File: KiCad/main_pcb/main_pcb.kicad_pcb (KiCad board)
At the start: 2 copper layers, 130 x 100 mm, 61 parts, among them J1 Conn_01x07, J2 Conn_01x07, J3 Conn_01x13, J4 Conn_01x06, J5 Conn_01x02, J6 USB_C_Receptacle_USB2.0_14P, SW1 SW_Push, U1 TXB0104D, U2 TXB0104D, U3 TXB0104D, U4 ATmega2560-16A, U5 AMS1117-3.3, U7 CH340C, Y1 Crystal_GND24

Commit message: feat(PCB): Adds two pins header for LED Backlight
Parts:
- added J7: Conn_01x02, Connector_JST:JST_XH_B2B-XH-A_1x02_P2.50mm_Vertical, F.Cu at (120.2, 52.5)
- moved REF** 5.20 mm to (139.6, 115.3)
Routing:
- net /Screens/MAIN_SCREEN_BL-3V3: track 13.7 -> 27.3 mm, vias 2 -> 3

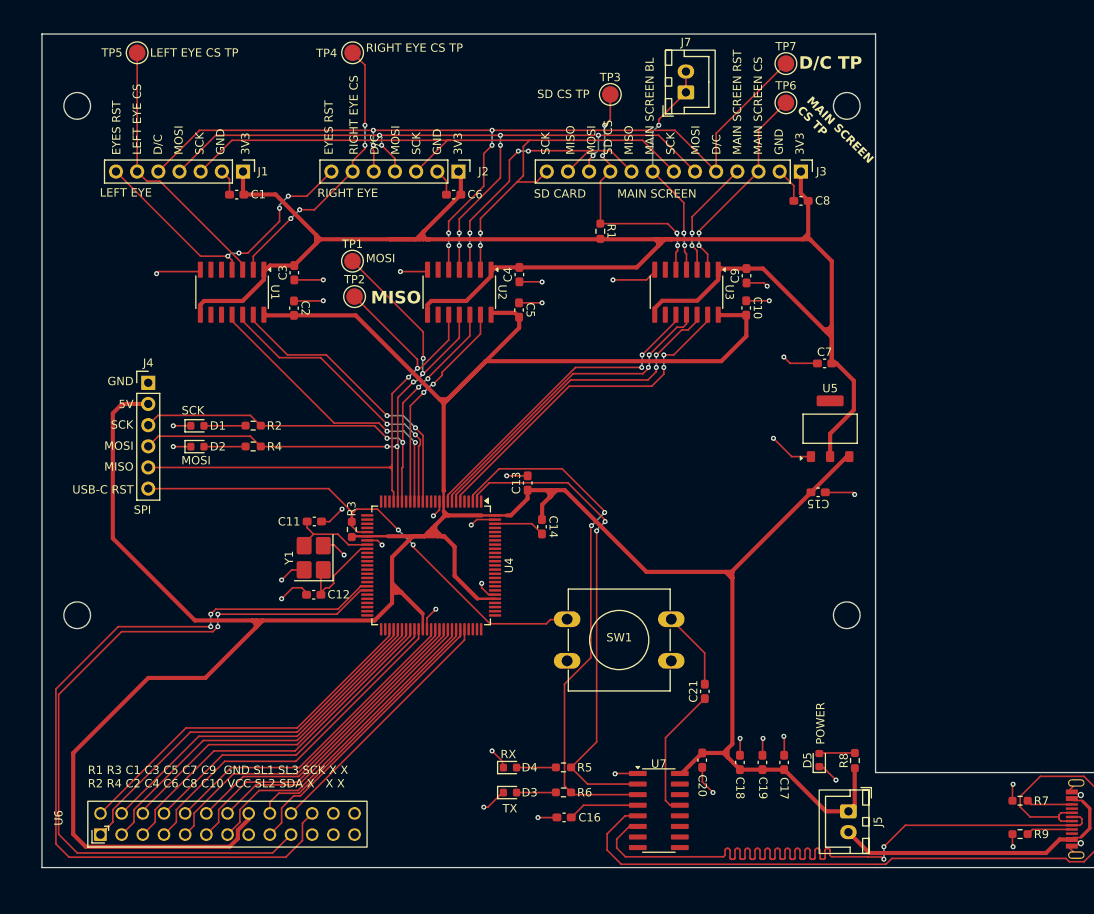
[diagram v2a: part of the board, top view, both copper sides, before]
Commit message: feat(pcb): Uses new footprint for Male Header 2x13
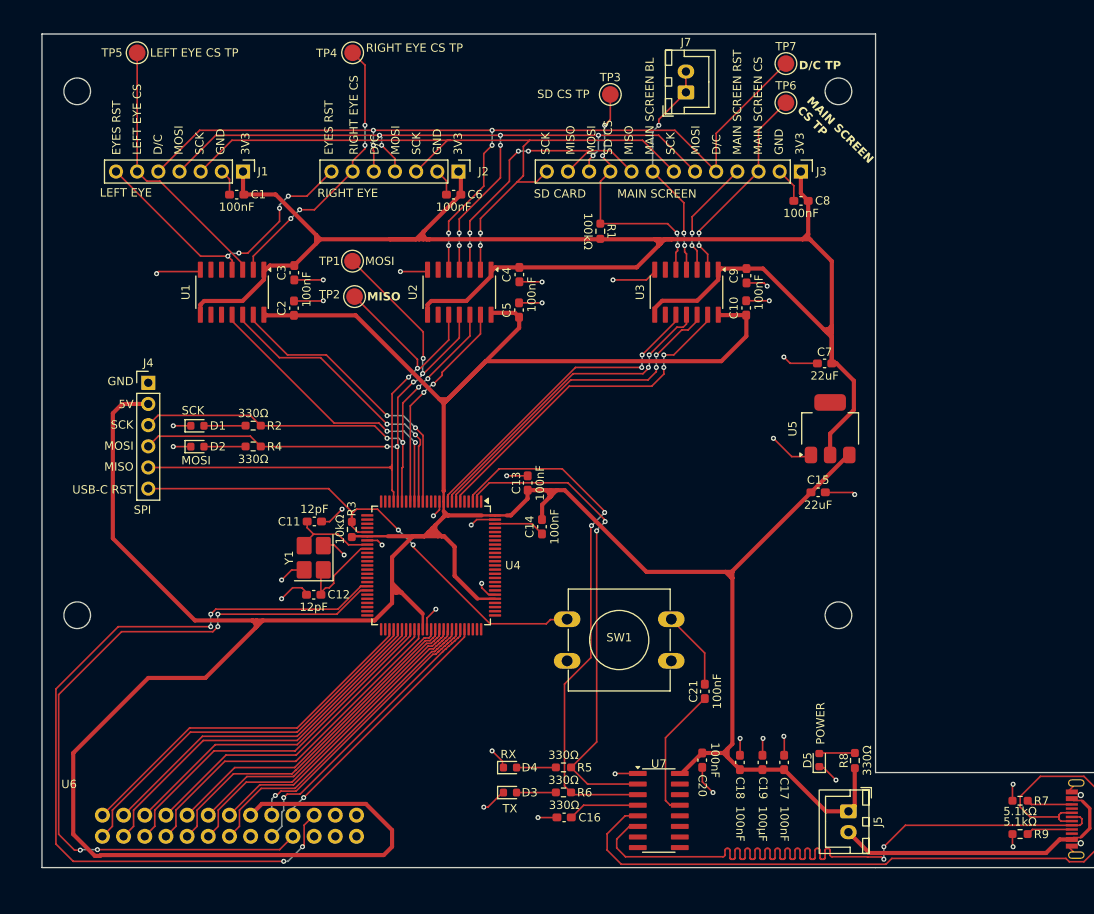
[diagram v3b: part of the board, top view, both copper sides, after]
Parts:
- U5: footprint Lilibrary:SOT-223-3_TabPin2_AMS1117 -> Package_TO_SOT_SMD:SOT-223-3_TabPin2
- U6: footprint Lilibrary:male_header -> Lilibrary:IDC-TH_26P-P2.54_OMRON_XG4C-2631
- moved U6 20.0 mm to (65.5, 140.5)
- moved REF** 2.02 mm to (138.6, 52.4)
- moved REF** 1.75 mm to (47.2, 52.4)
- moved REF** 1.00 mm to (138.6, 115.3)
- turned U5 to 90 degrees
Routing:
- net VCC: track 397.5 -> 433.5 mm
- net /SDL_SW2: track 35.5 -> 34.6 mm, vias 0 -> 1
- net /SCL: track 97.6 -> 98.3 mm, vias 2 -> 4
- net /SDA: track 89.6 -> 89.4 mm, vias 2 -> 4
- net /SDL_SW1: track 32.8 -> 32.7 mm, vias 0 -> 1
- net /SDL_SW3: track 30.7 -> 30.8 mm, vias 0 -> 1
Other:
- board text added: "100kΩ"
- board text added: "100nF"
- board text added: "100µF"
- board text added: "10kΩ"
- board text added: "12pF"
- board text added: "22uF"
- board text added: "330Ω"
- board text added: "5.1kΩ"
- board text removed: "R1 R3 C1 C3 C5 C7 C9 GND SL1 SL3 SCK X X R2 R4 C2 C4 C6 C8 C10 VCC SL2 SDA X X X"

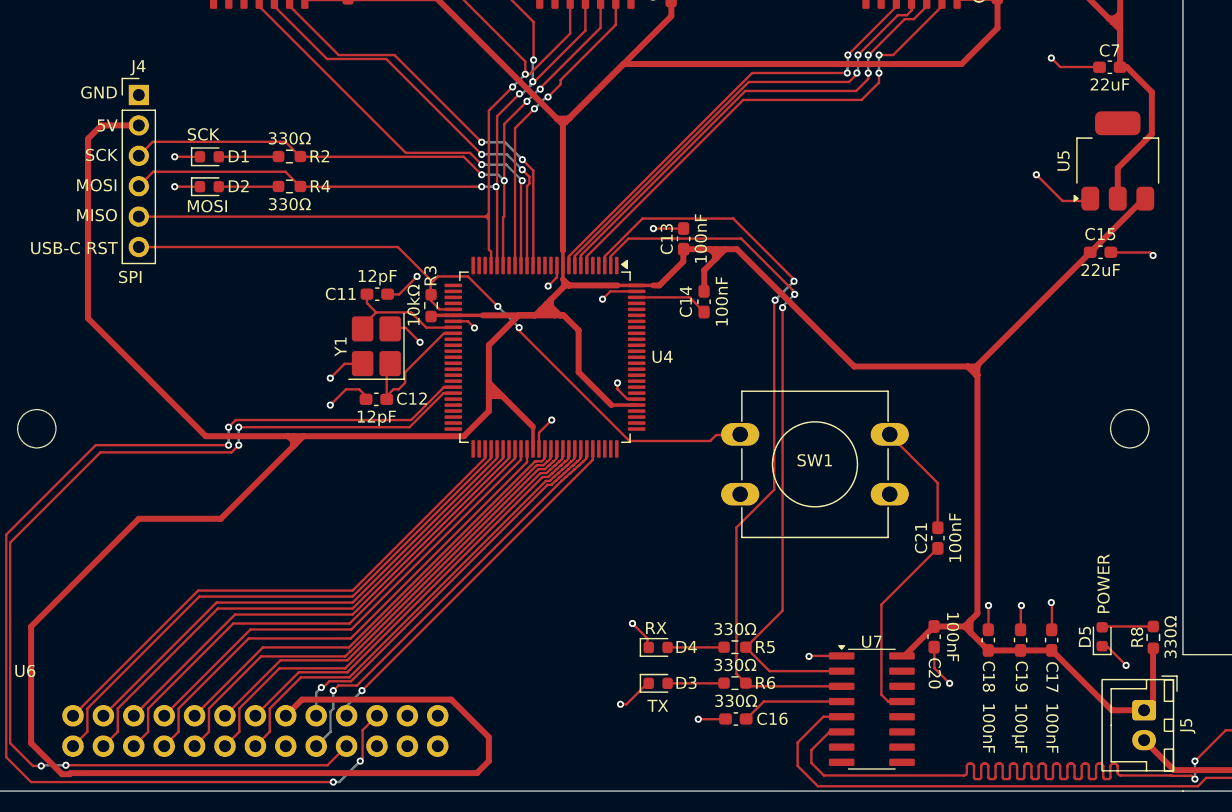
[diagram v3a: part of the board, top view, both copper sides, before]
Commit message: feat(3D models): Adds 3D models to PCB
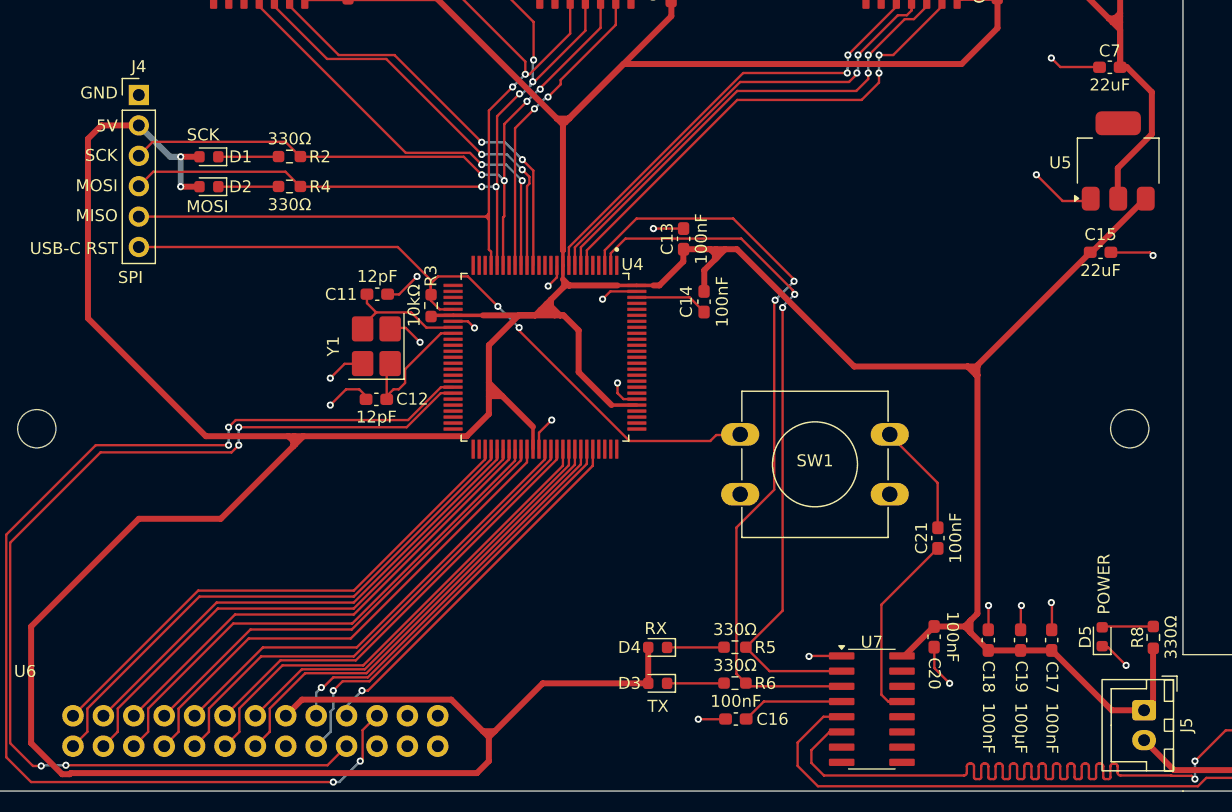
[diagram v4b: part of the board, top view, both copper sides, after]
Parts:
- U4: footprint Package_QFP:TQFP-100_14x14mm_P0.5mm -> Lilibrary:ATmega2560-16AU
- U5: footprint Package_TO_SOT_SMD:SOT-223-3_TabPin2 -> Lilibrary:SOT-223-3_TabPin2_AMS1117
- Y1: footprint Crystal:Crystal_SMD_3225-4Pin_3.2x2.5mm_HandSoldering -> Lilibrary:Crystal_3225
- turned D1 to 180 degrees
- turned D2 to 180 degrees
- turned D3 to 180 degrees
- turned D4 to 180 degrees
- turned U5 to 0 degrees
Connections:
- D1 pad 1: GND -> Net-(D1-K)
- D1 pad 2: Net-(D1-A) -> VCC
- D2 pad 1: GND -> Net-(D2-K)
- D2 pad 2: Net-(D2-A) -> VCC
- D3 pad 1: GND -> Net-(D3-K)
- D3 pad 2: Net-(D3-A) -> VCC
- D4 pad 1: GND -> Net-(D4-K)
- D4 pad 2: Net-(D4-A) -> VCC
- R2 pad 2: Net-(D1-A) -> Net-(D1-K)
- R4 pad 2: Net-(D2-A) -> Net-(D2-K)
- R5 pad 2: Net-(D4-A) -> Net-(D4-K)
- R6 pad 2: Net-(D3-A) -> Net-(D3-K)
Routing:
- net VCC: track 433.5 -> 463.4 mm, vias 0 -> 2
- net GND: track 117.2 -> 107.9 mm, vias 35 -> 31
- net Net-(D2-K): track 0.00 -> 4.92 mm
- net Net-(D2-A): track 4.92 -> 0.00 mm
- net Net-(D1-K): track 0.00 -> 4.92 mm
- net Net-(D1-A): track 4.92 -> 0.00 mm
- net Net-(D4-K): track 0.00 -> 4.65 mm
- net Net-(D4-A): track 4.65 -> 0.00 mm
- net Net-(D3-K): track 0.00 -> 4.65 mm
- net Net-(D3-A): track 4.65 -> 0.00 mm
- net /C3: track 39.6 -> 40.5 mm
- net /SDL_SW2: track 34.6 -> 35.5 mm
- net /C2: track 43.7 -> 44.6 mm
- net /R3: track 42.6 -> 43.4 mm
- net /R1: track 44.1 -> 44.9 mm
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
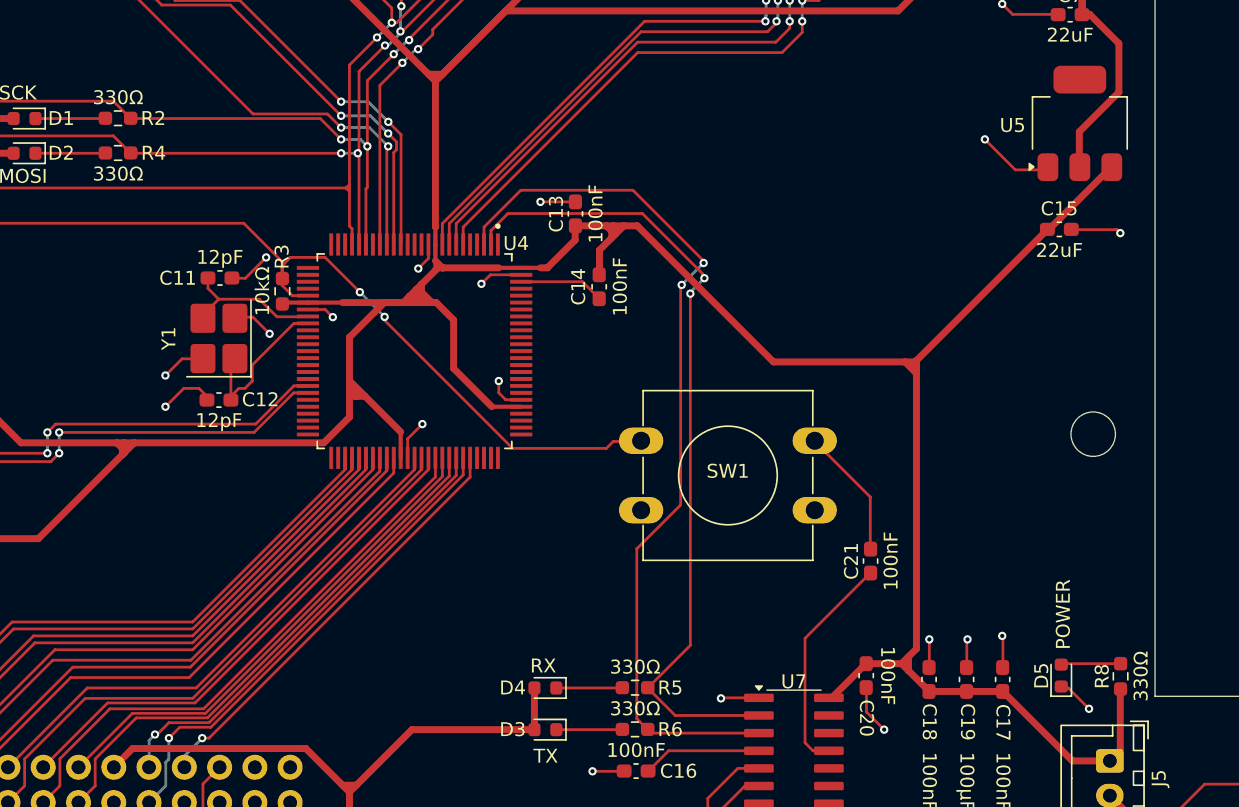
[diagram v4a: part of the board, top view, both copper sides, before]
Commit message: feat(schematic): Changes LED's resistor values from 330 ohms to 1k ohms.
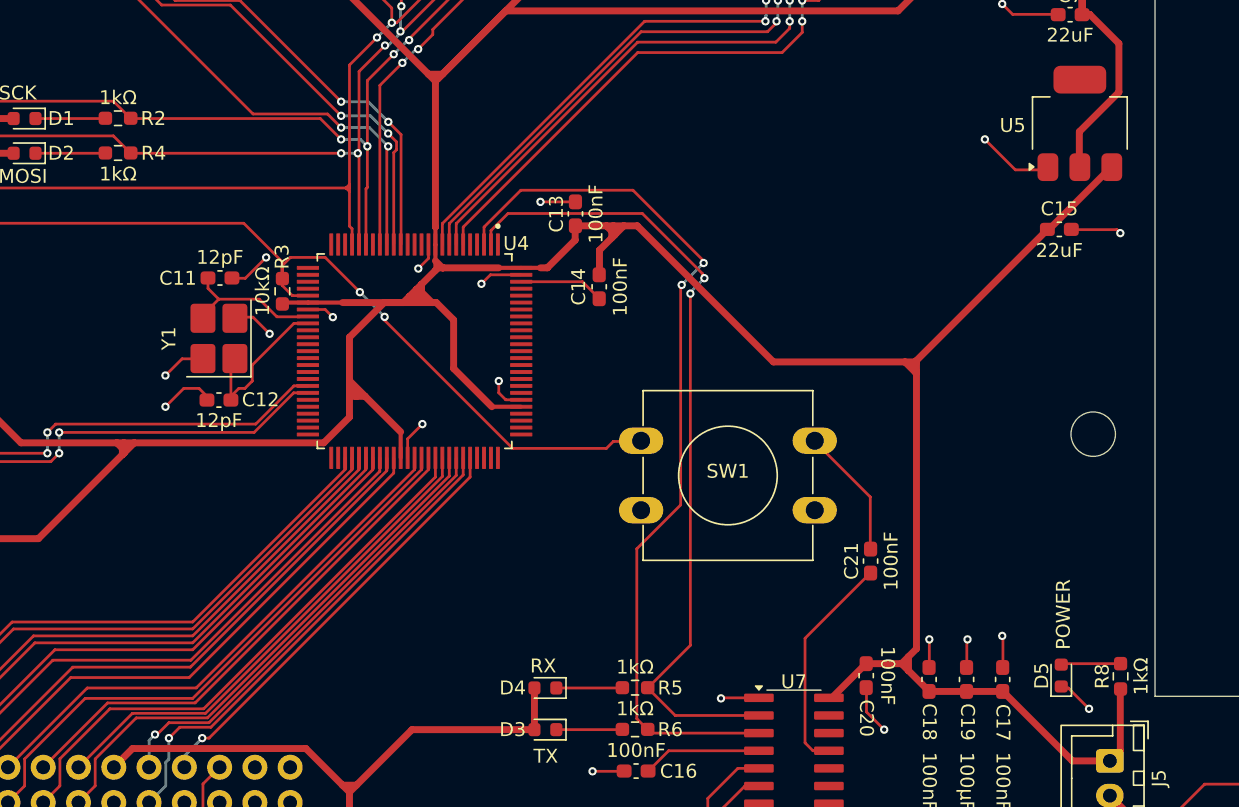
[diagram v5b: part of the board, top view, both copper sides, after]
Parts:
- R2, R4, R5, R6, R8: value 330Ω -> 1kΩ
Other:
- board text added: "1kΩ"
- board text removed: "330Ω"
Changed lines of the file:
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@@
 			)
 		)
-		(property "Value" "330Ω"
+		(property "Value" "1kΩ"
 			(at 0 1 180)
 			(unlocked yes)
@@
 			)
 		)
-		(property "LCSC" "C2933198"
+		(property "LCSC" "C22548"
 			(at 0 0 180)
 			(unlocked yes)
@@
 			)
 		)
-		(property "Value" "330Ω"
+		(property "Value" "1kΩ"
 			(at 0 1 180)
 			(unlocked yes)
@@
 			)
 		)
-		(property "LCSC" "C2933198"
+		(property "LCSC" "C22548"
 			(at 0 0 180)
 			(unlocked yes)
@@
 			)
 		)
-		(property "Value" "330Ω"
+		(property "Value" "1kΩ"
 			(at 0 1 180)
 			(unlocked yes)
@@
 			)
 		)
-		(property "LCSC" "C2933198"
+		(property "LCSC" "C22548"
 			(at 0 0 180)
 			(unlocked yes)
@@
 			)
 		)
-		(property "Value" "330Ω"
+		(property "Value" "1kΩ"
 			(at 0 1 90)
 			(unlocked yes)
@@
 			)
 		)
-		(property "LCSC" "C2933198"
+		(property "LCSC" "C22548"
 			(at 0 0 90)
 			(unlocked yes)
@@
 			)
 		)
-		(property "Value" "330Ω"
+		(property "Value" "1kΩ"
 			(at 0 1 180)
 			(unlocked yes)
@@
 			)
 		)
-		(property "LCSC" "C2933198"
+		(property "LCSC" "C22548"
 			(at 0 0 180)
 			(unlocked yes)
@@
 		)
 	)
-	(gr_text "330Ω"
+	(gr_text "1kΩ"
 		(at 68.3375 91 0)
 		(layer "F.SilkS")
@@
 		)
 	)
-	(gr_text "330Ω"
+	(gr_text "1kΩ"
 		(at 68.3375 96.5 0)
 		(layer "F.SilkS")
@@
 		)
 	)
-	(gr_text "330Ω"
+	(gr_text "1kΩ"
 		(at 105.5625 132 0)
 		(layer "F.SilkS")
@@
 		)
 	)
-	(gr_text "330Ω"
+	(gr_text "1kΩ"
 		(at 105.5625 135 0)
 		(layer "F.SilkS")
@@
 		)
 	)
-	(gr_text "330Ω"
+	(gr_text "1kΩ"
 		(at 142 132.6625 90)
 		(layer "F.SilkS")
@@
 		(name "$teardrop_padvia$")
 		(hatch none 0.1)
-		(priority 30002)
+		(priority 30007)
 		(attr
 			(teardrop
@@
 		(name "$teardrop_padvia$")
 		(hatch none 0.1)
-		(priority 30363)
+		(priority 30010)
 		(attr
 			(teardrop
@@
 		(name "$teardrop_padvia$")
 		(hatch none 0.1)
-		(priority 30002)
+		(priority 30013)
 		(attr
 			(teardrop
@@
 		(name "$teardrop_padvia$")
 		(hatch none 0.1)
-		(priority 30126)
+		(priority 30002)
 		(attr
 			(teardrop
@@
 		(name "$teardrop_padvia$")
 		(hatch none 0.1)
-		(priority 30364)
+		(priority 30011)
 		(attr
 			(teardrop
@@
 		(name "$teardrop_padvia$")
 		(hatch none 0.1)
-		(priority 30001)
+		(priority 30003)
 		(attr
 			(teardrop
@@
 		(name "$teardrop_padvia$")
 		(hatch none 0.1)
-		(priority 30001)
+		(priority 30008)
 		(attr
 			(teardrop
@@
 		(name "$teardrop_padvia$")
 		(hatch none 0.1)
-		(priority 30365)
+		(priority 30012)
 		(attr
 			(teardrop
@@
 		(name "$teardrop_padvia$")
 		(hatch none 0.1)
-		(priority 30367)
+		(priority 30014)
 		(attr
 			(teardrop
@@
 		(name "$teardrop_padvia$")
 		(hatch none 0.1)
-		(priority 30001)
+		(priority 30009)
 		(attr
 			(teardrop
@@
 		(name "$teardrop_padvia$")
 		(hatch none 0.1)
-		(priority 30000)
+		(priority 30001)
 		(attr
 			(teardrop
@@
 		(name "$teardrop_padvia$")
 		(hatch none 0.1)
-		(priority 30207)
+		(priority 30006)
 		(attr
 			(teardrop
@@
 		(name "$teardrop_padvia$")
 		(hatch none 0.1)
-		(priority 30001)
+		(priority 30004)
 		(attr
 			(teardrop
@@
 		(name "$teardrop_padvia$")
 		(hatch none 0.1)
-		(priority 30000)
+		(priority 30002)
 		(attr
 			(teardrop
@@
 		(name "$teardrop_padvia$")
 		(hatch none 0.1)
-		(priority 30000)
+		(priority 30003)
 		(attr
 			(teardrop
@@
 		(name "$teardrop_padvia$")
 		(hatch none 0.1)
-		(priority 30368)
+		(priority 30015)
 		(attr
 			(teardrop
@@
 		(name "$teardrop_padvia$")
 		(hatch none 0.1)
-		(priority 30002)
+		(priority 30010)
 		(attr
 			(teardrop
@@
 		(name "$teardrop_padvia$")
 		(hatch none 0.1)
-		(priority 30125)
+		(priority 30001)
 		(attr
 			(teardrop
@@
 		(name "$teardrop_padvia$")
 		(hatch none 0.1)
-		(priority 30369)
+		(priority 30016)
 		(attr
 			(teardrop
@@
 		(name "$teardrop_padvia$")
 		(hatch none 0.1)
-		(priority 30370)
+		(priority 30017)
 		(attr
 			(teardrop
@@
 		(name "$teardrop_padvia$")
 		(hatch none 0.1)
-		(priority 30209)
+		(priority 30008)
 		(attr
 			(teardrop
@@
 		(name "$teardrop_padvia$")
 		(hatch none 0.1)
-		(priority 30205)
+		(priority 30004)
 		(attr
 			(teardrop
@@
 		(name "$teardrop_padvia$")
 		(hatch none 0.1)
-		(priority 30208)
+		(priority 30007)
 		(attr
 			(teardrop
@@
 		(name "$teardrop_padvia$")
 		(hatch none 0.1)
-		(priority 30002)
+		(priority 30011)
 		(attr
 			(teardrop
@@
 		(name "$teardrop_padvia$")
 		(hatch none 0.1)
-		(priority 30210)
+		(priority 30009)
 		(attr
 			(teardrop
@@
 		(name "$teardrop_padvia$")
 		(hatch none 0.1)
-		(priority 30206)
+		(priority 30005)
 		(attr
 			(teardrop
@@
 		(name "$teardrop_padvia$")
 		(hatch none 0.1)
-		(priority 30371)
+		(priority 30018)
 		(attr
 			(teardrop
@@
 		(name "$teardrop_padvia$")
 		(hatch none 0.1)
-		(priority 30366)
+		(priority 30013)
 		(attr
 			(teardrop
@@
 		(name "$teardrop_padvia$")
 		(hatch none 0.1)
-		(priority 30001)
+		(priority 30012)
 		(attr
 			(teardrop
